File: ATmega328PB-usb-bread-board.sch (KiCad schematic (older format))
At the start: 34 parts, among them J1 Conn_01x17, J2 Conn_01x17, J3 USB_B_Micro, J4 AVR-ISP-6, J5 Grove-I2C-connector, J6 Grove-I2C-connector, J7 Grove-I2C-connector, U1 ATmega328PB-MU, U2 CP2102N-A01-GQFN28, U3 LMV358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

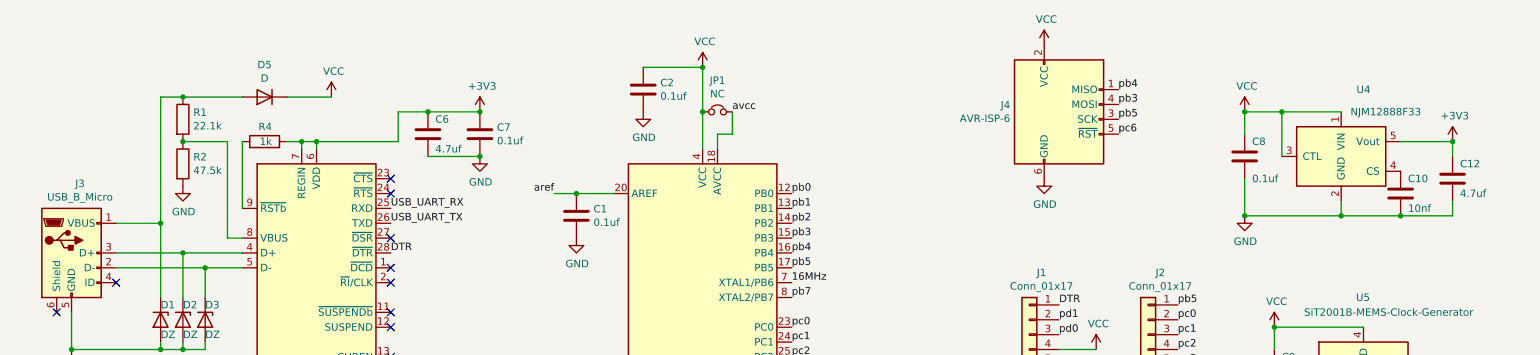
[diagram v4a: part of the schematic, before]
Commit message: Use cp2102 as 3v3 regulator
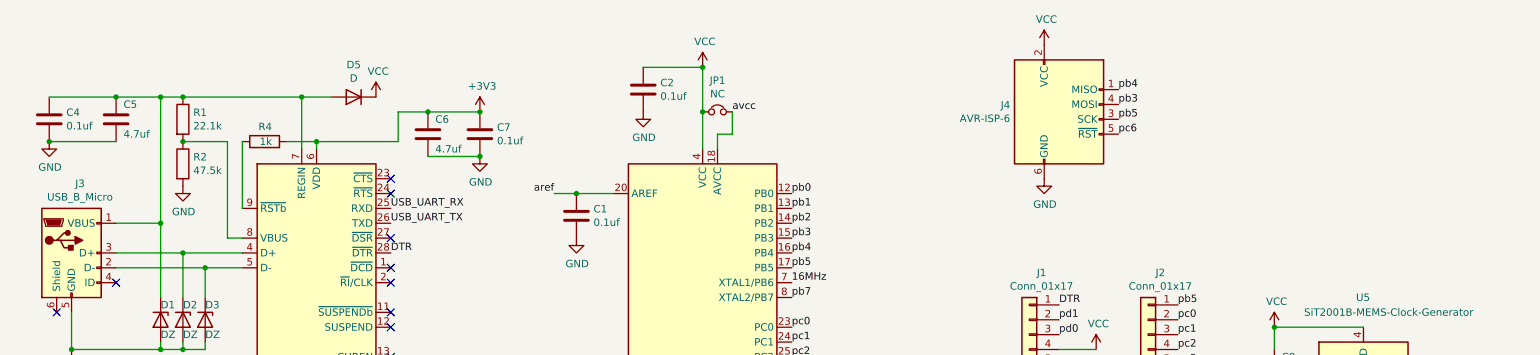
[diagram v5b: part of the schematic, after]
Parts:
- removed C10: 10nf, Capacitor_SMD:C_0603_1608Metric, symbol Device:C
- removed C12: 4.7uf, Capacitor_SMD:C_0402_1005Metric, symbol Device:C
- removed C8: 0.1uf, Capacitor_SMD:C_0603_1608Metric, symbol Device:C
- removed U4: NJM12888F33, Package_TO_SOT_SMD:SOT-23-5, symbol my-kicad-symbols:NJM12888F33
- added C4: 0.1uf, Capacitor_SMD:C_0603_1608Metric, symbol Device:C
- added C5: 4.7uf, Capacitor_SMD:C_0402_1005Metric, symbol Device:C
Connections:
- net +3V3: no longer U2.7 (REGIN)
- net GND: now also C4.2, C5.2
- net at D1.1 (K), D5.2 (A), J3.1 (VBUS)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: now also U2.7 (REGIN), C4.1, C5.1
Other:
- moved on the sheet: D5
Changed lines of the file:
@@
 Connection ~ 4700 6450
-$Comp
-L Device:D D5
-U 1 1 5F87D197
-P 2600 1400
-F 0 "D5" H 2600 1183 50  0000 C CNN
-F 1 "D" H 2600 1274 50  0000 C CNN
-F 2 "Diode_SMD:D_SOD-123F" H 2600 1400 50  0001 C CNN
-F 3 "~" H 2600 1400 50  0001 C CNN
-	1    2600 1400
-	-1   0    0    1
-$EndComp
-$Comp
-L power:VCC #PWR0123
-U 1 1 5F87D6DB
-P 3050 1400
-F 0 "#PWR0123" H 3050 1250 50  0001 C CNN
-F 1 "VCC" H 3065 1573 50  0000 C CNN
-F 2 "" H 3050 1400 50  0001 C CNN
-F 3 "" H 3050 1400 50  0001 C CNN
-	1    3050 1400
-	1    0    0    -1
-$EndComp
 $Comp
 L power:+3V3 #PWR0126
@@
 	2450 1700 2450 2150
 Wire Wire Line
-	2750 1700 2850 1700
-Wire Wire Line
 	2950 1700 2950 1750
+Text Label 3450 2450 0    50   ~ 0
+DTR
+Wire Wire Line
+	1150 1700 1600 1700
+$Comp
+L power:GND #PWR0129
+U 1 1 5F9017BB
+P 1150 1700
+F 0 "#PWR0129" H 1150 1450 50  0001 C CNN
+F 1 "GND" H 1155 1527 50  0000 C CNN
+F 2 "" H 1150 1700 50  0001 C CNN
+F 3 "" H 1150 1700 50  0001 C CNN
+	1    1150 1700
+	1    0    0    -1
+$EndComp
+Connection ~ 1150 1700
+$Comp
+L Device:C C4
+U 1 1 5F9005EE
+P 1150 1550
+F 0 "C4" H 1265 1596 50  0000 L CNN
+F 1 "0.1uf" H 1265 1505 50  0000 L CNN
+F 2 "Capacitor_SMD:C_0603_1608Metric" H 1188 1400 50  0001 C CNN
+F 3 "~" H 1150 1550 50  0001 C CNN
+	1    1150 1550
+	1    0    0    -1
+$EndComp
+$Comp
+L Device:C C5
+U 1 1 5F8FC33B
+P 1600 1550
+F 0 "C5" H 1650 1650 50  0000 L CNN
+F 1 "4.7uf" H 1650 1450 50  0000 L CNN
+F 2 "Capacitor_SMD:C_0402_1005Metric" H 1638 1400 50  0001 C CNN
+F 3 "~" H 1600 1550 50  0001 C CNN
+	1    1600 1550
+	1    0    0    -1
+$EndComp
+Wire Wire Line
+	2750 1700 2950 1700
+Wire Wire Line
+	2850 1400 3050 1400
+Wire Wire Line
+	2850 1400 2850 1750
+$Comp
+L power:VCC #PWR0123
+U 1 1 5F87D6DB
+P 3350 1400
+F 0 "#PWR0123" H 3350 1250 50  0001 C CNN
+F 1 "VCC" H 3365 1573 50  0000 C CNN
+F 2 "" H 3350 1400 50  0001 C CNN
+F 3 "" H 3350 1400 50  0001 C CNN
+	1    3350 1400
+	1    0    0    -1
+$EndComp
+$Comp
+L Device:D D5
+U 1 1 5F87D197
+P 3200 1400
+F 0 "D5" H 3200 1183 50  0000 C CNN
+F 1 "D" H 3200 1274 50  0000 C CNN
+F 2 "Diode_SMD:D_SOD-123F" H 3200 1400 50  0001 C CNN
+F 3 "~" H 3200 1400 50  0001 C CNN
+	1    3200 1400
+	-1   0    0    1
+$EndComp
+Connection ~ 2850 1400
+Connection ~ 2050 1400
+Wire Wire Line
+	2050 1400 2850 1400
+Connection ~ 1900 1400
+Wire Wire Line
+	1900 1400 1600 1400
+Wire Wire Line
+	1600 1400 1150 1400
+Connection ~ 1600 1400
 $Comp
 L Device:C C6
@@
 Wire Wire Line
 	3500 1700 3500 1500
+Connection ~ 2950 1700
 Wire Wire Line
 	3500 1500 3700 1500
-Connection ~ 2950 1700
+Wire Wire Line
+	3700 1500 4050 1500
 Connection ~ 3700 1500
-Wire Wire Line
-	3700 1500 4050 1500
-Wire Wire Line
-	2050 1400 2450 1400
-Connection ~ 2050 1400
-$Comp
-L power:+3V3 #PWR0129
-U 1 1 5F92FD3C
+$Comp
+L power:+3V3 #PWR?
+U 1 1 5F9873FD
 P 4050 1500
-F 0 "#PWR0129" H 4050 1350 50  0001 C CNN
+F 0 "#PWR?" H 4050 1350 50  0001 C CNN
 F 1 "+3V3" H 4065 1673 50  0000 C CNN
 F 2 "" H 4050 1500 50  0001 C CNN
@@
 $EndComp
 Connection ~ 4050 1500
-Wire Wire Line
-	10600 2200 10600 2100
-Wire Wire Line
-	10600 1700 10250 1700
-Wire Wire Line
-	10600 1700 10600 1800
-Connection ~ 10600 1700
-$Comp
-L power:+3V3 #PWR0125
-U 1 1 5F8D6BD8
-P 10600 1700
-F 0 "#PWR0125" H 10600 1550 50  0001 C CNN
-F 1 "+3V3" H 10615 1873 50  0000 C CNN
-F 2 "" H 10600 1700 50  0001 C CNN
-F 3 "" H 10600 1700 50  0001 C CNN
-	1    10600 1700
-	1    0    0    -1
-$EndComp
-$Comp
-L Device:C C12
-U 1 1 5F8D5F68
-P 10600 1950
-F 0 "C12" H 10650 2050 50  0000 L CNN
-F 1 "4.7uf" H 10650 1850 50  0000 L CNN
-F 2 "Capacitor_SMD:C_0402_1005Metric" H 10638 1800 50  0001 C CNN
-F 3 "~" H 10600 1950 50  0001 C CNN
-	1    10600 1950
-	1    0    0    -1
-$EndComp
-Wire Wire Line
-	9850 2200 9850 2100
-Connection ~ 9850 2200
-Wire Wire Line
-	9200 2200 9850 2200
-Wire Wire Line
-	9200 1950 9200 2200
-Wire Wire Line
-	10250 2200 10600 2200
-Wire Wire Line
-	9850 2200 10250 2200
-Connection ~ 10250 2200
-$Comp
-L Device:C C10
-U 1 1 5F8D0B51
-P 10250 2050
-F 0 "C10" H 10300 2150 50  0000 L CNN
-F 1 "10nf" H 10300 1950 50  0000 L CNN
-F 2 "Capacitor_SMD:C_0603_1608Metric" H 10288 1900 50  0001 C CNN
-F 3 "~" H 10250 2050 50  0001 C CNN
-	1    10250 2050
-	1    0    0    -1
-$EndComp
-Wire Wire Line
-	9200 1650 9200 1500
-Wire Wire Line
-	9450 1500 9850 1500
-Wire Wire Line
-	9450 1500 9450 1800
-Connection ~ 9450 1500
-Wire Wire Line
-	9200 1500 9450 1500
-$Comp
-L Device:C C8
-U 1 1 5F8C87B4
-P 9200 1800
-F 0 "C8" H 9250 1900 50  0000 L CNN
-F 1 "0.1uf" H 9250 1650 50  0000 L CNN
-F 2 "Capacitor_SMD:C_0603_1608Metric" H 9238 1650 50  0001 C CNN
-F 3 "~" H 9200 1800 50  0001 C CNN
-	1    9200 1800
-	1    0    0    -1
-$EndComp
-Connection ~ 9200 2200
-$Comp
-L power:GND #PWR0124
-U 1 1 5F8C7AD0
-P 9200 2200
-F 0 "#PWR0124" H 9200 1950 50  0001 C CNN
-F 1 "GND" H 9205 2027 50  0000 C CNN
-F 2 "" H 9200 2200 50  0001 C CNN
-F 3 "" H 9200 2200 50  0001 C CNN
-	1    9200 2200
-	1    0    0    -1
-$EndComp
-Connection ~ 9200 1500
-$Comp
-L power:VCC #PWR0111
-U 1 1 5F8C761A
-P 9200 1500
-F 0 "#PWR0111" H 9200 1350 50  0001 C CNN
-F 1 "VCC" H 9215 1673 50  0000 C CNN
-F 2 "" H 9200 1500 50  0001 C CNN
-F 3 "" H 9200 1500 50  0001 C CNN
-	1    9200 1500
-	1    0    0    -1
-$EndComp
-$Comp
-L my-kicad-symbols:NJM12888F33 U4
-U 1 1 5F8C64C1
-P 9850 1800
-F 0 "U4" H 10000 2250 50  0000 C CNN
-F 1 "NJM12888F33" H 10150 2100 50  0000 C CNN
-F 2 "Package_TO_SOT_SMD:SOT-23-5" H 9850 1800 50  0001 C CNN
-F 3 "" H 9850 1800 50  0001 C CNN
-	1    9850 1800
-	1    0    0    -1
-$EndComp
-Wire Wire Line
-	2750 1400 3050 1400
-Wire Wire Line
-	2850 1700 2850 1750
-Connection ~ 2850 1700
-Wire Wire Line
-	2850 1700 2950 1700
-Text Label 3450 2450 0    50   ~ 0
-DTR
 $EndSCHEMATC
